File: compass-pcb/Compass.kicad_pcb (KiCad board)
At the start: 2 copper layers, 17 parts

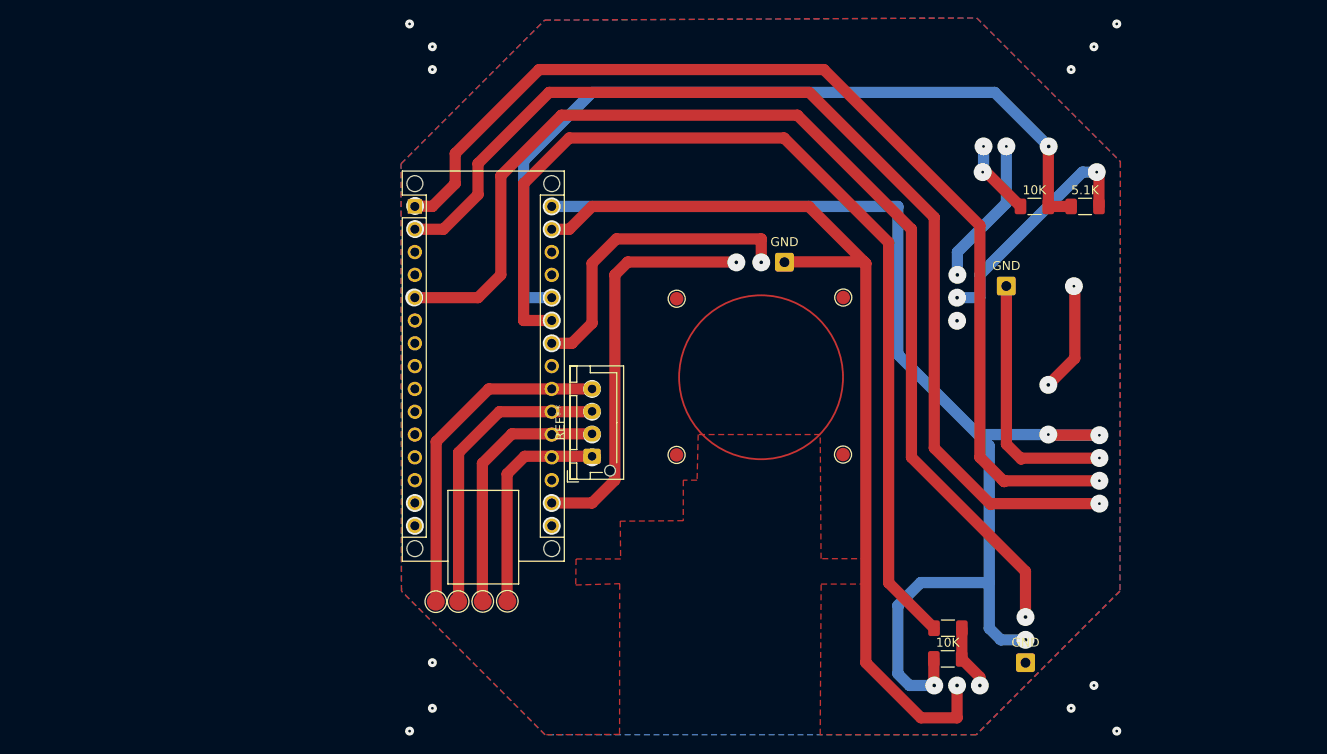
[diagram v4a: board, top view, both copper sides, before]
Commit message: Larger through holes
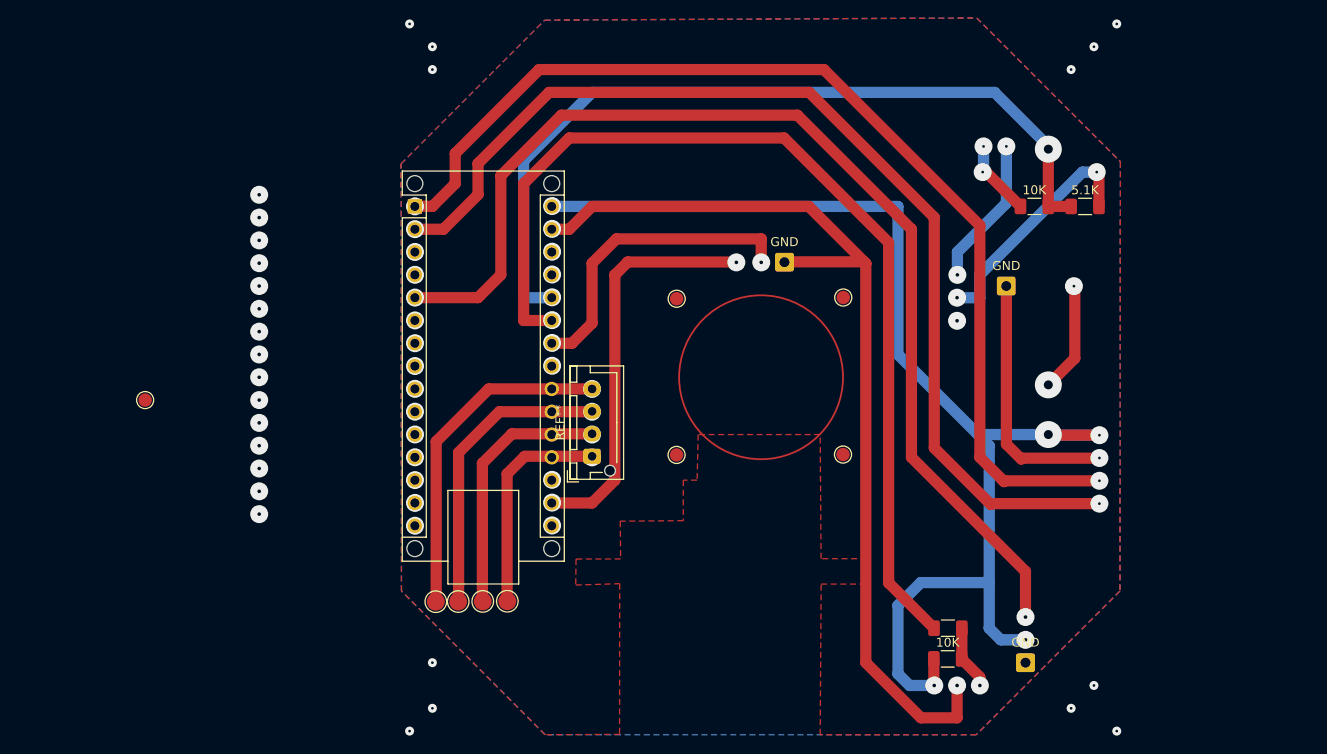
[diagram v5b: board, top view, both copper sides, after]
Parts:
- added REF**: , TestPoint:TestPoint_Pad_D1.5mm, F.Cu at (78.7, 96.5)
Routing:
- net (no net): vias 47 -> 76
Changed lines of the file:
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@@
     (pad "1" smd circle (at 0 0) (size 2 2) (layers "F.Cu" "F.Mask"))
+  )
+  (footprint "TestPoint:TestPoint_Pad_D1.5mm" (layer "F.Cu")
+    (at 78.74 96.52)
+    (descr "SMD pad as test Point, diameter 1.5mm")
+    (tags "test point SMD pad")
+    (attr exclude_from_pos_files exclude_from_bom)
+    (fp_text reference "REF**" (at 2.54 -10.158) (layer "F.SilkS") hide
+        (effects (font (size 1 1) (thickness 0.15)))
+    )
+    (fp_text value " " (at 0 1.75) (layer "F.Fab")
+        (effects (font (size 1 1) (thickness 0.15)))
+    )
+    (fp_circle (center 0 0) (end 0 0.95)
+      (stroke (width 0.12) (type solid)) (fill none) (layer "F.SilkS"))
+    (fp_circle (center 0 0) (end 1.25 0)
+      (stroke (width 0.05) (type solid)) (fill none) (layer "F.CrtYd"))
+    (pad " " smd circle (at 0 0) (size 1.5 1.5) (layers "F.Cu" "F.Mask")
+      (zone_connect 0))
+    (pad " " smd circle (at 0 0) (size 1.5 1.5) (layers "F.Cu" "F.Mask")
+      (zone_connect 0))
   )
   (gr_circle (center 147.32 93.98) (end 156.445445 93.98)
@@
   (segment (start 128.505445 97.818533) (end 118.188967 97.818533) (width 1.25) (layer "F.Cu") (net 0))
   (via (at 172.092894 68.275233) (size 2) (drill 0.3) (layers "F.Cu" "B.Cu") (net 0))
-  (via (at 179.347506 68.283233) (size 2) (drill 0.4) (layers "F.Cu" "B.Cu") (net 0))
-  (via (at 108.798645 74.904016) (size 2) (drill 0.4) (layers "F.Cu" "B.Cu") (net 0))
-  (via (at 124.013168 87.658533) (size 2) (drill 0.4) (layers "F.Cu" "B.Cu") (net 0))
+  (via (at 91.44 99.06) (size 2) (drill 0.4) (layers "F.Cu" "B.Cu") (net 0))
   (via (at 108.185445 133.378533) (size 1) (drill 0.3) (layers "F.Cu" "B.Cu") (net 0))
-  (via (at 108.699687 85.096606) (size 2) (drill 0.4) (layers "F.Cu" "B.Cu") (net 0))
+  (via (at 108.787292 82.56937) (size 2) (drill 0.4) (layers "F.Cu" "B.Cu") (net 0))
   (via (at 110.725445 125.758533) (size 1) (drill 0.3) (layers "F.Cu" "B.Cu") (net 0))
-  (via (at 124.013168 85.118533) (size 2) (drill 0.4) (layers "F.Cu" "B.Cu") (net 0))
+  (via (at 179.305445 94.827562) (size 3) (drill 1) (layers "F.Cu" "B.Cu") (net 0))
+  (via (at 124.053119 107.936758) (size 2) (drill 0.4) (layers "F.Cu" "B.Cu") (net 0))
+  (via (at 124.053119 105.396758) (size 2) (drill 0.4) (layers "F.Cu" "B.Cu") (net 0))
+  (via (at 124.053119 74.916758) (size 2) (drill 0.4) (layers "F.Cu" "B.Cu") (net 0))
+  (via (at 108.787292 102.88937) (size 2) (drill 0.4) (layers "F.Cu" "B.Cu") (net 0))
+  (via (at 108.787292 92.72937) (size 2) (drill 0.4) (layers "F.Cu" "B.Cu") (net 0))
+  (via (at 124.053119 82.536758) (size 2) (drill 0.4) (layers "F.Cu" "B.Cu") (net 0))
   (via (at 166.605445 128.298533) (size 2) (drill 0.4) (layers "F.Cu" "B.Cu") (net 0))
+  (via (at 108.787292 90.18937) (size 2) (drill 0.4) (layers "F.Cu" "B.Cu") (net 0))
+  (via (at 91.44 81.28) (size 2) (drill 0.4) (layers "F.Cu" "B.Cu") (net 0))
   (via (at 181.845445 130.838533) (size 1) (drill 0.3) (layers "F.Cu" "B.Cu") (net 0))
-  (via (at 124.013168 107.978533) (size 2) (drill 0.4) (layers "F.Cu" "B.Cu") (net 0))
-  (via (at 124.013168 90.198533) (size 2) (drill 0.4) (layers "F.Cu" "B.Cu") (net 0))
+  (via (at 108.787292 107.96937) (size 2) (drill 0.4) (layers "F.Cu" "B.Cu") (net 0))
+  (via (at 91.44 78.74) (size 2) (drill 0.4) (layers "F.Cu" "B.Cu") (net 0))
   (via (at 182.156358 83.835847) (size 2) (drill 0.3) (layers "F.Cu" "B.Cu") (net 0))
-  (via (at 108.773168 110.518533) (size 2) (drill 0.3) (layers "F.Cu" "B.Cu") (net 0))
+  (via (at 108.787292 85.10937) (size 2) (drill 0.4) (layers "F.Cu" "B.Cu") (net 0))
+  (via (at 91.44 76.2) (size 2) (drill 0.4) (layers "F.Cu" "B.Cu") (net 0))
   (via (at 110.725445 130.838533) (size 1) (drill 0.3) (layers "F.Cu" "B.Cu") (net 0))
+  (via (at 108.787292 100.34937) (size 2) (drill 0.4) (layers "F.Cu" "B.Cu") (net 0))
   (via (at 186.925445 133.378533) (size 1) (drill 0.3) (layers "F.Cu" "B.Cu") (net 0))
-  (via (at 108.773168 107.978533) (size 2) (drill 0.3) (layers "F.Cu" "B.Cu") (net 0))
   (via (at 184.993201 105.506017) (size 2) (drill 0.3) (layers "F.Cu" "B.Cu") (net 0))
   (via (at 169.180526 82.578533) (size 2) (drill 0.4) (layers "F.Cu" "B.Cu") (net 0))
-  (via (at 124.013168 74.958533) (size 2) (drill 0.4) (layers "F.Cu" "B.Cu") (net 0))
+  (via (at 91.44 93.98) (size 2) (drill 0.4) (layers "F.Cu" "B.Cu") (net 0))
+  (via (at 91.44 73.66) (size 2) (drill 0.4) (layers "F.Cu" "B.Cu") (net 0))
+  (via (at 91.44 83.82) (size 2) (drill 0.4) (layers "F.Cu" "B.Cu") (net 0))
+  (via (at 108.787292 87.64937) (size 2) (drill 0.4) (layers "F.Cu" "B.Cu") (net 0))
   (via (at 184.385445 128.298533) (size 1) (drill 0.3) (layers "F.Cu" "B.Cu") (net 0))
   (via (at 144.570556 81.187222) (size 2) (drill 0.4) (layers "F.Cu" "B.Cu") (net 0))
-  (via (at 124.013168 110.518533) (size 2) (drill 0.3) (layers "F.Cu" "B.Cu") (net 0))
+  (via (at 124.053119 79.996758) (size 2) (drill 0.4) (layers "F.Cu" "B.Cu") (net 0))
   (via (at 176.765445 123.218533) (size 2) (drill 0.4) (layers "F.Cu" "B.Cu") (net 0))
+  (via (at 108.787292 95.26937) (size 2) (drill 0.4) (layers "F.Cu" "B.Cu") (net 0))
   (via (at 147.341357 81.187222) (size 2) (drill 0.4) (layers "F.Cu" "B.Cu") (net 0))
+  (via (at 124.053119 87.616758) (size 2) (drill 0.4) (layers "F.Cu" "B.Cu") (net 0))
+  (via (at 124.053119 85.076758) (size 2) (drill 0.4) (layers "F.Cu" "B.Cu") (net 0))
+  (via (at 124.053119 92.696758) (size 2) (drill 0.4) (layers "F.Cu" "B.Cu") (net 0))
   (via (at 181.845445 59.718533) (size 1) (drill 0.3) (layers "F.Cu" "B.Cu") (net 0))
   (via (at 176.765445 120.678533) (size 2) (drill 0.4) (layers "F.Cu" "B.Cu") (net 0))
@@
   (via (at 169.145445 87.69142) (size 2) (drill 0.4) (layers "F.Cu" "B.Cu") (net 0))
   (via (at 169.145445 85.118533) (size 2) (drill 0.4) (layers "F.Cu" "B.Cu") (free) (net 0))
-  (via (at 179.305445 100.358533) (size 2) (drill 0.3) (layers "F.Cu" "B.Cu") (net 0))
+  (via (at 179.305445 100.358533) (size 3) (drill 1) (layers "F.Cu" "B.Cu") (net 0))
+  (via (at 91.44 101.6) (size 2) (drill 0.4) (layers "F.Cu" "B.Cu") (net 0))
   (via (at 174.632894 68.275233) (size 2) (drill 0.3) (layers "F.Cu" "B.Cu") (net 0))
+  (via (at 108.787292 77.48937) (size 2) (drill 0.4) (layers "F.Cu" "B.Cu") (net 0))
+  (via (at 91.44 88.9) (size 2) (drill 0.4) (layers "F.Cu" "B.Cu") (net 0))
+  (via (at 91.44 91.44) (size 2) (drill 0.4) (layers "F.Cu" "B.Cu") (net 0))
+  (via (at 91.44 109.22) (size 2) (drill 0.4) (layers "F.Cu" "B.Cu") (net 0))
   (via (at 171.685445 128.298533) (size 2) (drill 0.4) (layers "F.Cu" "B.Cu") (net 0))
   (via (at 128.505445 97.818533) (size 2) (drill 0.3) (layers "F.Cu" "B.Cu") (free) (net 0))
-  (via (at 108.798645 77.476903) (size 2) (drill 0.4) (layers "F.Cu" "B.Cu") (net 0))
   (via (at 184.993201 100.431017) (size 2) (drill 0.3) (layers "F.Cu" "B.Cu") (net 0))
+  (via (at 91.44 106.68) (size 2) (drill 0.4) (layers "F.Cu" "B.Cu") (net 0))
   (via (at 184.696358 71.135847) (size 2) (drill 0.3) (layers "F.Cu" "B.Cu") (net 0))
+  (via (at 108.787292 105.42937) (size 2) (drill 0.4) (layers "F.Cu" "B.Cu") (net 0))
+  (via (at 179.305445 68.58) (size 3) (drill 1) (layers "F.Cu" "B.Cu") (net 0))
+  (via (at 124.053119 90.156758) (size 2) (drill 0.4) (layers "F.Cu" "B.Cu") (net 0))
+  (via (at 108.787292 80.02937) (size 2) (drill 0.4) (layers "F.Cu" "B.Cu") (net 0))
   (via (at 128.505445 102.898533) (size 2) (drill 0.3) (layers "F.Cu" "B.Cu") (net 0))
+  (via (at 91.44 104.14) (size 2) (drill 0.4) (layers "F.Cu" "B.Cu") (net 0))
+  (via (at 91.44 96.52) (size 2) (drill 0.4) (layers "F.Cu" "B.Cu") (net 0))
   (via (at 186.925445 54.638533) (size 1) (drill 0.3) (layers "F.Cu" "B.Cu") (net 0))
   (via (at 184.385445 57.178533) (size 1) (drill 0.3) (layers "F.Cu" "B.Cu") (net 0))
-  (via (at 179.305445 94.827562) (size 2) (drill 0.4) (layers "F.Cu" "B.Cu") (net 0))
   (via (at 128.505445 100.353533) (size 2) (drill 0.3) (layers "F.Cu" "B.Cu") (net 0))
   (via (at 108.185445 54.638533) (size 1) (drill 0.3) (layers "F.Cu" "B.Cu") (net 0))
+  (via (at 124.053119 110.476758) (size 2) (drill 0.4) (layers "F.Cu" "B.Cu") (net 0))
+  (via (at 108.787292 97.80937) (size 2) (drill 0.4) (layers "F.Cu" "B.Cu") (net 0))
   (via (at 184.993201 108.051017) (size 2) (drill 0.3) (layers "F.Cu" "B.Cu") (net 0))
+  (via (at 91.44 86.36) (size 2) (drill 0.4) (layers "F.Cu" "B.Cu") (net 0))
   (via (at 128.505445 95.278533) (size 2) (drill 0.3) (layers "F.Cu" "B.Cu") (net 0))
   (via (at 171.996358 71.135847) (size 2) (drill 0.3) (layers "F.Cu" "B.Cu") (net 0))
+  (via (at 108.787292 110.50937) (size 2) (drill 0.4) (layers "F.Cu" "B.Cu") (net 0))
   (via (at 110.725445 59.718533) (size 1) (drill 0.3) (layers "F.Cu" "B.Cu") (net 0))
+  (via (at 108.787292 74.94937) (size 2) (drill 0.4) (layers "F.Cu" "B.Cu") (net 0))
   (segment (start 120.885445 85.118533) (end 124.013168 85.118533) (width 1.25) (layer "B.Cu") (net 0))
   (segment (start 172.72 116.84) (end 172.72 121.92) (width 1.25) (layer "B.Cu") (net 0))
@@
   (via (at 169.145445 128.298533) (size 2) (drill 0.4) (layers "F.Cu" "B.Cu") (net 1))
   (via (at 184.993201 102.971017) (size 2) (drill 0.3) (layers "F.Cu" "B.Cu") (net 1))
-  (via (at 124.013168 77.498533) (size 2) (drill 0.4) (layers "F.Cu" "B.Cu") (net 1))
+  (via (at 124.053119 77.456758) (size 2) (drill 0.4) (layers "F.Cu" "B.Cu") (net 1))
   (segment (start 184.883296 102.861112) (end 184.993201 102.971017) (width 1.25) (layer "B.Cu") (net 1))
   (zone (net 1) (net_name "GND") (layer "F.Cu") (hatch edge 0.5)

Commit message: bigger pads for holes where possible, additional support under Arduino
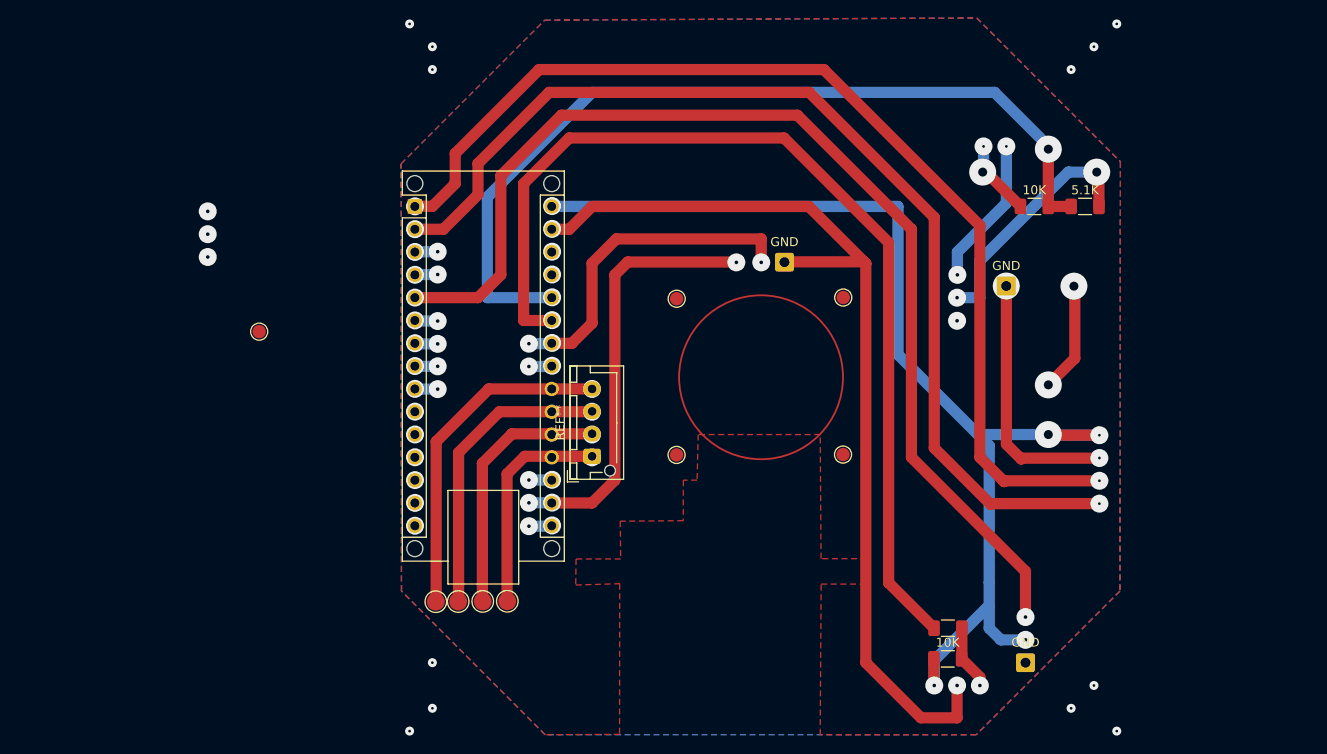
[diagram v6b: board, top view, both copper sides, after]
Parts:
- moved REF** 14.8 mm to (91.4, 88.9)
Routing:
- net (no net): track 980.3 -> 1003.2 mm, vias 76 -> 75
- net GND: vias 3 -> 4

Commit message: expanding footprint for small dots where possible
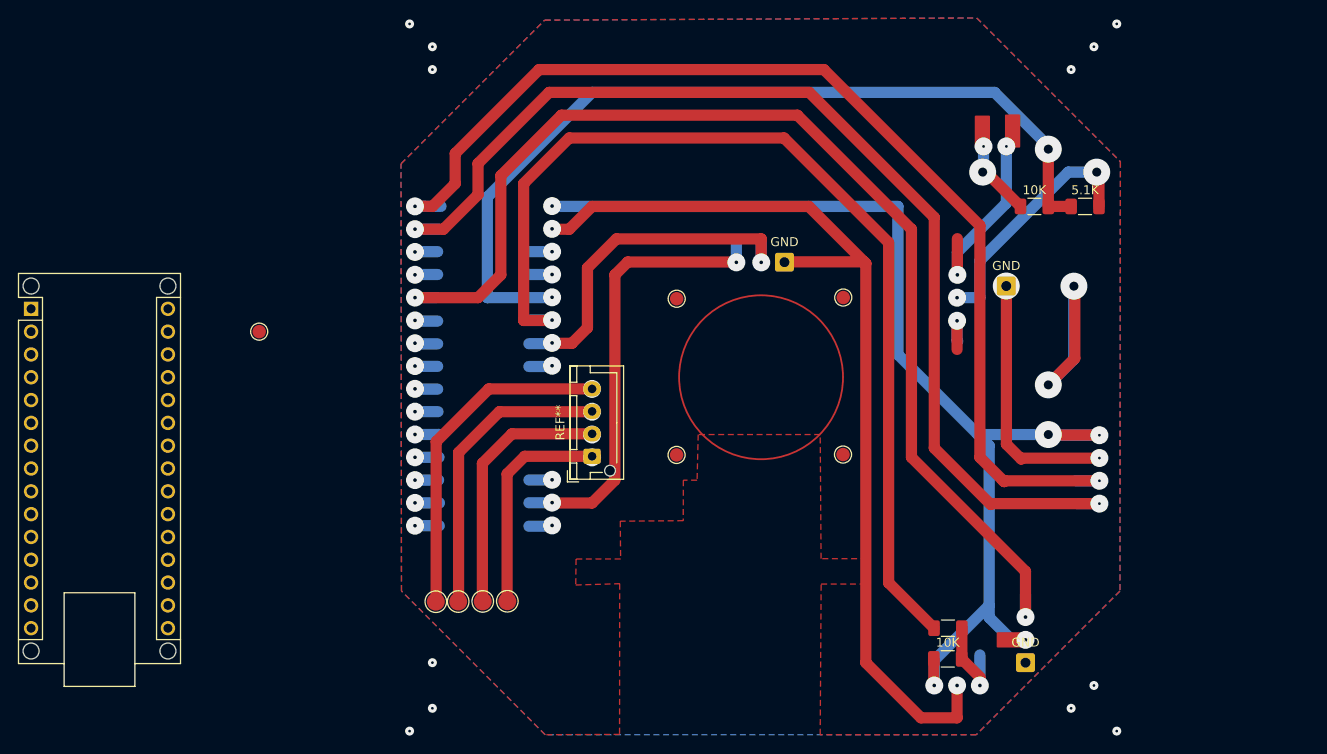
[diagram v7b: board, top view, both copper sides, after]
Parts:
- moved REF** 44.2 mm to (66.0, 86.4)
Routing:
- net (no net): track 1003.2 -> 1072.1 mm, vias 75 -> 61

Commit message: polishing layout
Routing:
- net (no net): track 1072.1 -> 1122.2 mm
- net GND: vias 4 -> 3
